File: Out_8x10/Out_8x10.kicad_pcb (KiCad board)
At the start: 2 copper layers, 100 x 100 mm, 382 parts, among them J1 Conn_01x06, J10 Conn_01x06, J11 Conn_01x06, J2 nmount JST 1mm QWIIC, J2 nmount SW Debug, J3 USB_C_Receptacle_USB2.0, J3 nmount SW Debug, J4 Conn_01x06, J4 USB_C_Receptacle_USB2.0, J5 Conn_01x06, J5 Conn_01x09, J6 Conn_01x06, J6 Conn_01x10, J7 Conn_01x06, J7 Conn_01x09, J8 Conn_01x06, J8 Conn_01x12, J9 Conn_01x06, Q1 2N7002, Q10 2N7002, Q10 AO3401A, Q11 2N7002, Q11 AO3401A, Q12 2N7002, Q12 AO3401A, Q13 2N7002, Q13 AO3400A, Q14 2N7002, Q14 AO3400A, Q15 AO3400A, Q15 AO3401A, Q16 AO3400A, Q16 AO3401A, Q17 2N7002, Q17 AO3400A, Q18 2N7002, Q18 AO3400A, Q19 2N7002, Q19 AO3400A, Q2 2N7002, Q20 2N7002, Q20 AO3400A, Q21 2N7002, Q21 AO3400A, Q22 2N7002, Q22 AO3400A, Q23 2N7002, Q23 AO3400A, Q24 2N7002, Q24 AO3400A, Q25 AO3400A, Q25 IRLR3410, Q26 AO3400A, Q26 IRLR3410, Q27 IRLR3410, Q28 IRLR3410, Q29 IRLR3410, Q3 2N7002, Q30 IRLR3410, Q31 IRLR3410, Q32 IRLR3410, Q4 2N7002, Q4 AO3401A, Q5 2N7002, Q5 AO3401A, Q6 2N7002, Q6 AO3401A, Q7 2N7002, Q8 2N7002, Q9 2N7002, SW1 Reset, SW2 Boot, SW3 ADDRESS, U1 ADM3483, U10 L78L24_SOT89, U11 L78L24_SOT89, U12 L78L24_SOT89, U13 L78L24_SOT89, U2 W25Q128JVSIQ, U3 RP2040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

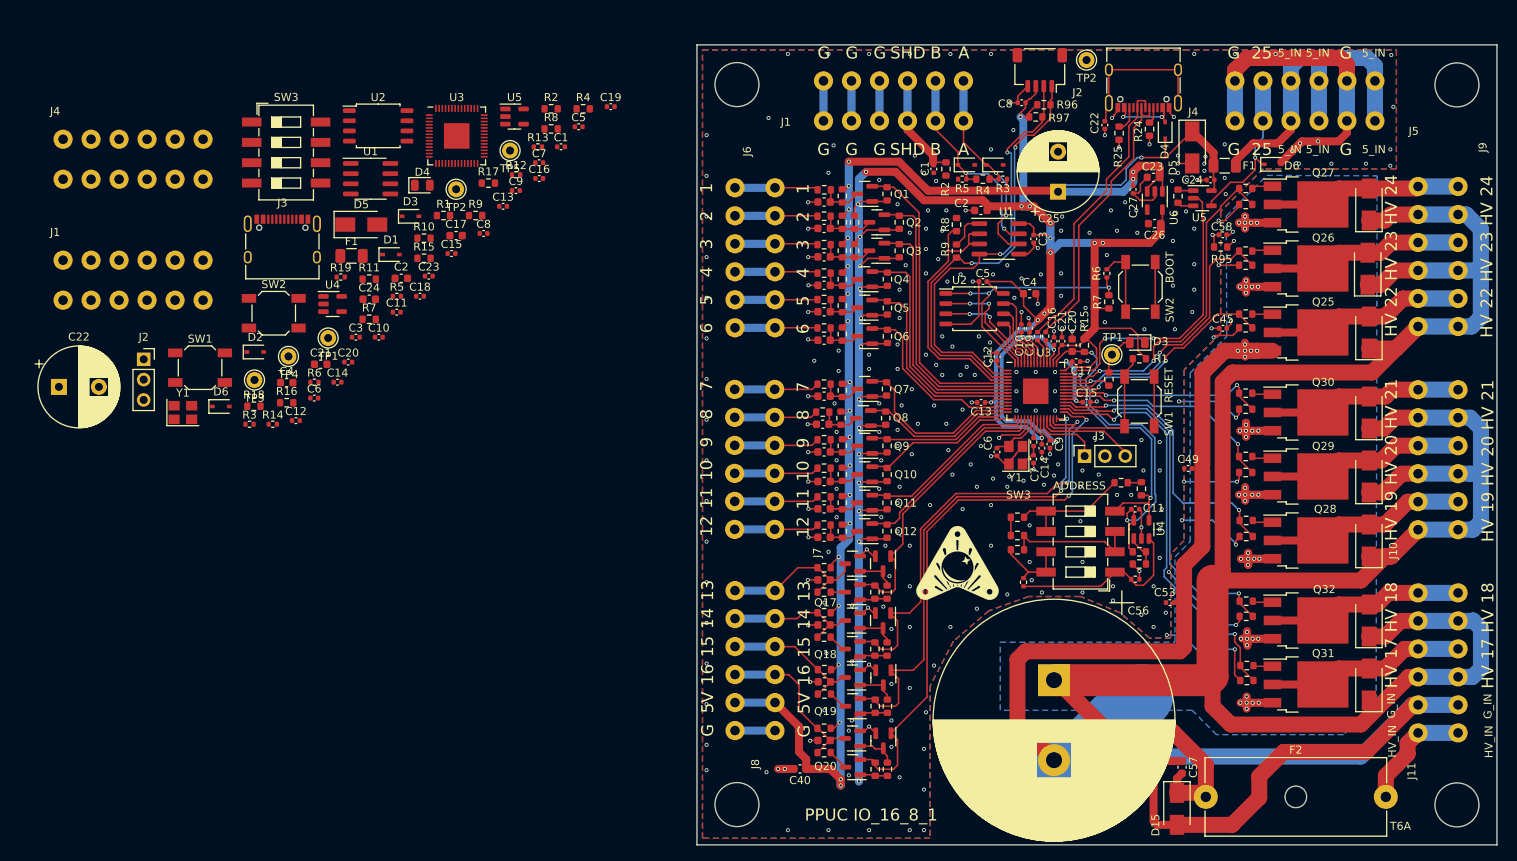
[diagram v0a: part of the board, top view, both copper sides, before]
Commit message: updated layout
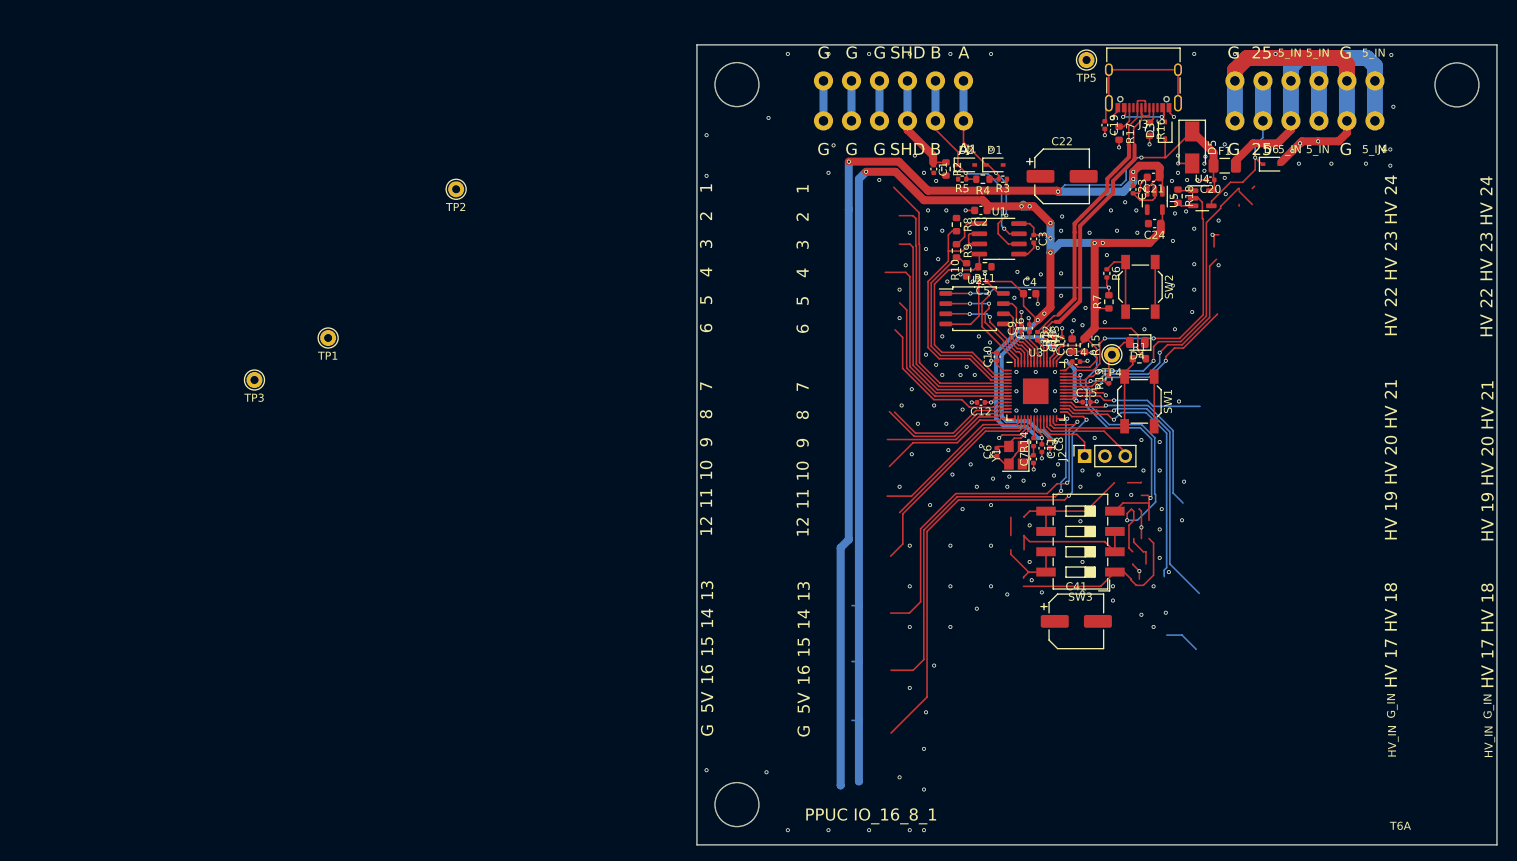
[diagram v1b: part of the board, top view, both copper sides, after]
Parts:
- removed the C1 at (132.8, 60.3)
- removed the C10 at (143.7, 80.2)
- removed the C11 at (158.0, 102.8)
- removed the C12 at (140.7, 83.8)
- removed the C13 at (138.7, 89.5)
- removed the C14 at (146.3, 95.2)
- removed the C15 at (151.9, 89.4)
- removed the C16 at (147.8, 81.8)
- removed the C17 at (150.6, 84.4)
- removed the C19 at (144.8, 80.2)
- removed the C2 at (138.7, 65.5)
- removed the C20 at (150.1, 82.3)
- removed the C21 at (148.8, 81.8)
- removed the C22 at (154.2, 54.8)
- removed the C23 at (160.3, 61.3)
- removed the C24 at (167.4, 61.7)
- removed the C25 at (148.3, 63.1)
- removed the C26 at (160.4, 67.1)
- removed the C27 at (157.7, 62.9)
- removed the C28 at (119.1, 64.4)
- removed the C29 at (119.1, 67.7)
- removed the C3 at (145.3, 69.0)
- removed the C30 at (119.1, 71.3)
- removed the C31 at (119.1, 74.8)
- removed the C32 at (119.1, 78.1)
- removed the C33 at (119.1, 81.7)
- removed the C34 at (119.1, 88.7)
- removed the C35 at (118.9, 92.2)
- removed the C36 at (119.1, 95.7)
- removed the C37 at (119.1, 99.4)
- removed the C38 at (119.1, 102.8)
- removed the C39 at (119.1, 106.3)
- removed the C4 at (144.8, 75.9)
- removed the C40 at (116.1, 135.3)
- removed C42, C43, C44: 470p, Capacitor_SMD:C_0603_1608Metric
- removed C45, C49, C53, C58: 100n, Capacitor_SMD:C_0402_1005Metric
- removed the C5 at (138.9, 74.4)
- removed C56: 3300µ 63V, Capacitor_THT:CP_Radial_D30.0mm_P10.00mm_SnapIn
- removed C57: 100n 50V, Capacitor_SMD:C_0603_1608Metric
- removed the C6 at (140.7, 95.7)
- removed the C7 at (145.3, 96.6)
- removed the C8 at (143.8, 52.0)
- removed the C9 at (147.3, 94.7)
- removed the D1 at (140.4, 59.8)
- removed D10, D11, D12, D13, D14, D7, D8, D9: MRA4004T3G, Diode_SMD:D_SMA
- removed D15: SMAJ60, Diode_SMD:D_SMA
- removed the D2 at (136.9, 59.8)
- removed the D3 at (158.2, 82.0)
- removed the D4 at (161.7, 55.5)
- removed the D5 at (165.1, 57.6)
- removed the D6 at (43.7, 90.0)
- removed the D6 at (175.2, 59.7)
- removed the F1 at (169.2, 59.9)
- removed F2: T6A, Fuse:Fuseholder_Cylinder-5x20mm_Schurter_0031_8201_Horizontal_Open
- removed the J1 at (136.5, 49.3)
- removed J10, J11, J9: Conn_01x06, IO_16_8_1:Terminal_Block_RTMPin
- removed the J2 at (146.1, 47.9)
- removed the J3 at (151.7, 96.2)
- removed the J4 at (159.0, 49.0)
- removed the J5 at (187.9, 49.3)
- removed the J6 at (108.0, 62.6)
- removed the J7 at (107.9, 87.8)
- removed the J8 at (108.0, 113.0)
- removed the Q1 at (124.2, 63.4)
- removed the Q10 at (124.2, 98.5)
- removed the Q11 at (124.2, 102.0)
- removed the Q12 at (124.2, 105.6)
- removed the Q13 at (122.6, 109.6)
- removed the Q14 at (122.6, 116.7)
- removed the Q15 at (122.6, 123.9)
- removed the Q16 at (122.6, 131.5)
- removed the Q17 at (122.6, 113.2)
- removed the Q18 at (122.6, 120.3)
- removed the Q19 at (122.7, 127.4)
- removed the Q2 at (125.7, 67.0)
- removed the Q20 at (122.7, 135.1)
- removed the Q21 at (126.5, 109.6)
- removed the Q22 at (126.5, 116.7)
- removed the Q23 at (126.5, 123.9)
- removed the Q24 at (126.5, 131.8)
- removed the Q25 at (179.3, 80.7)
- removed the Q26 at (179.3, 72.7)
- removed Q27, Q28, Q29, Q30, Q31, Q32: IRLR3410, Package_TO_SOT_SMD:TO-252-3_TabPin4
- removed the Q3 at (125.7, 70.5)
- removed the Q4 at (124.2, 74.1)
- removed the Q5 at (124.2, 77.6)
- removed the Q6 at (124.2, 81.2)
- removed the Q7 at (124.2, 87.8)
- removed the Q8 at (124.0, 91.4)
- removed the Q9 at (124.2, 94.9)
- removed the R1 at (158.5, 84.0)
- removed the R10 at (145.8, 81.2)
- removed the R11 at (146.8, 81.2)
- removed the R12 at (145.3, 94.4)
- removed the R13 at (158.5, 108.1)
- removed the R14 at (158.5, 109.7)
- removed the R15 at (151.6, 82.3)
- removed the R16 at (158.0, 111.6)
- removed the R17 at (158.8, 100.3)
- removed the R18 at (143.3, 106.1)
- removed the R19 at (143.3, 107.9)
- removed the R2 at (134.3, 60.3)
- removed the R20 at (144.0, 112.0)
- removed the R21 at (154.7, 86.6)
- removed the R22 at (156.2, 99.5)
- removed the R23 at (143.3, 103.8)
- removed the R24 at (159.8, 55.3)
- removed the R25 at (156.0, 55.8)
- removed the R26 at (163.3, 63.7)
- removed the R27 at (119.1, 62.9)
- removed the R28 at (119.1, 66.2)
- removed the R29 at (119.1, 69.8)
- removed the R3 at (141.4, 61.6)
- removed the R30 at (119.1, 73.3)
- removed the R31 at (119.1, 76.6)
- removed the R32 at (119.1, 80.2)
- removed the R33 at (121.4, 63.7)
- removed the R34 at (121.4, 67.0)
- removed the R35 at (121.4, 70.5)
- removed the R36 at (121.4, 74.1)
- removed the R37 at (121.4, 77.4)
- removed the R38 at (121.4, 80.9)
- removed the R39 at (127.0, 63.4)
- removed the R4 at (138.9, 61.6)
- removed the R40 at (128.5, 67.0)
- removed the R41 at (128.5, 70.5)
- removed the R42 at (127.0, 74.1)
- removed the R43 at (127.0, 77.7)
- removed the R44 at (127.0, 81.2)
- removed the R45 at (119.1, 87.2)
- removed the R46 at (118.9, 90.7)
- removed the R47 at (119.1, 94.1)
- removed the R48 at (119.1, 97.7)
- removed the R49 at (119.1, 101.3)
- removed the R5 at (136.4, 61.6)
- removed the R50 at (119.1, 104.8)
- removed the R51 at (121.4, 88.0)
- removed the R52 at (121.2, 91.4)
- removed the R53 at (121.4, 94.9)
- removed the R54 at (121.4, 98.5)
- removed the R55 at (121.4, 102.0)
- removed R56, R57, R58, R59, R60, R61, R62, R63, R64, R65, R66, R71, R72, R73, R74, R75, R76, R77, R78, R79, R80, R81, R85, R86, R87, R91, R92, R96, R97: 10k, Resistor_SMD:R_0603_1608Metric
- removed the R6 at (154.4, 73.3)
- removed R67, R68, R69, R70: 330, Resistor_SMD:R_0603_1608Metric
- removed the R7 at (154.7, 76.9)
- removed the R8 at (135.6, 67.2)
- removed R82, R83, R84, R88, R89, R90, R93, R94, R95: 100R, Resistor_SMD:R_0603_1608Metric
- removed the R9 at (135.6, 70.5)
- removed R98, R99: nmount, Resistor_SMD:R_0603_1608Metric
- removed the REF** at (198.2, 139.8)
- removed the SW1 at (158.5, 89.3)
- removed the SW2 at (158.6, 75.0)
- removed the SW3 at (151.1, 106.9)
- removed the TP1 at (155.1, 83.5)
- removed the TP2 at (151.9, 46.7)
- removed the U1 at (141.0, 69.0)
- removed the U2 at (137.9, 77.8)
- removed the U3 at (145.5, 88.1)
- removed the U4 at (158.8, 105.3)
- removed the U5 at (166.4, 63.9)
- removed the U6 at (160.4, 64.2)
- removed the Y1 at (143.0, 96.1)
- added D6: SD05, Diode_SMD:D_SOD-323, F.Cu at (175.0, 59.7)
- C22: value 1000µ 10V -> 100µ 35V; footprint Capacitor_THT:CP_Radial_D10.0mm_P5.00mm -> Capacitor_SMD:CP_Elec_6.3x7.7
- C41: value 470p -> 100µ 35V; footprint Capacitor_SMD:C_0603_1608Metric -> Capacitor_SMD:CP_Elec_6.3x7.7
- moved J4 164.4 mm to (187.9, 49.3), turned to 180 degrees
- moved C22 128.1 mm to (148.8, 61.2)
- moved R18 118.5 mm to (163.3, 63.7), turned to -90 degrees
- moved J2 118.2 mm to (151.7, 96.2), turned to 90 degrees
- moved SW1 117.5 mm to (158.5, 89.3), turned to -90 degrees
- moved J1 115.8 mm to (136.5, 49.3), turned to 180 degrees
- moved R16 113.1 mm to (159.8, 55.3), turned to -90 degrees
- moved SW3 110.6 mm to (151.1, 106.9), turned to 180 degrees
- moved C20 110.2 mm to (167.4, 61.7), turned to 180 degrees
- moved F1 109.7 mm to (169.2, 59.9)
- moved J3 109.7 mm to (159.0, 49.0), turned to 180 degrees
- moved U4 109.5 mm to (166.4, 64.0)
- moved SW2 108.4 mm to (158.6, 75.0), turned to -90 degrees
- moved C21 106.7 mm to (160.3, 61.3), turned to 180 degrees
- moved D5 104.3 mm to (165.1, 57.6), turned to -90 degrees
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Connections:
- C41 pad 1: (no net) -> /20V
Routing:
- net (no net): track 2019.6 -> 4.42 mm, vias 75 -> 0
- net +3V3: track 333.3 -> 244.5 mm, vias 32 -> 15
- net GND: track 234.0 -> 161.2 mm, vias 287 -> 206
- net /Lo_8: track 0.00 -> 60.4 mm, vias 0 -> 2
- net /Lo_7: track 0.00 -> 50.7 mm, vias 0 -> 2
- net /DIP_1: track 0.00 -> 48.0 mm, vias 0 -> 1
- net /Lo_6: track 0.00 -> 46.1 mm, vias 0 -> 2
- net Net-(TP2-Pad1): track 0.00 -> 42.4 mm, vias 0 -> 2
- net +5V: track 200.4 -> 161.7 mm, vias 22 -> 5
- net /Lo_10: track 0.00 -> 36.7 mm, vias 0 -> 1
- net /Hi_1: track 0.00 -> 35.4 mm
- net Net-(TP3-Pad1): track 0.00 -> 33.1 mm, vias 0 -> 2
- net /Hi_2: track 0.00 -> 33.1 mm
- net /Lo_9: track 0.00 -> 33.0 mm, vias 0 -> 1
- net Net-(TP1-Pad1): track 0.00 -> 30.1 mm, vias 0 -> 2
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- removed copper zone on B.Cu, net (none)
- removed copper zone on B.Cu, net GND
- removed copper zone on F.Cu, net GND
